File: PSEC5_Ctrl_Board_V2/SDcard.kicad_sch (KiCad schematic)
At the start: 27 parts, among them J3 1040310811, J6 1040310811, Q1 NMOS, Q4 NMOS, U14 SIA427ADJ-T1-GE3, U17 TXS02612RTWR, U6 SIA427ADJ-T1-GE3

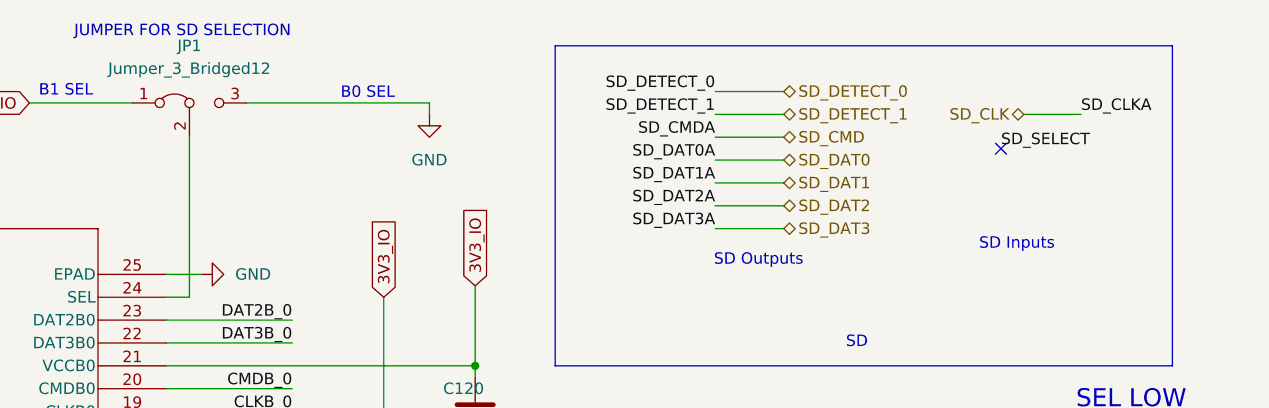
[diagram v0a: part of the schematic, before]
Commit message: Updated V2
New Power Planes, roruing of bottom samtec and kria positions
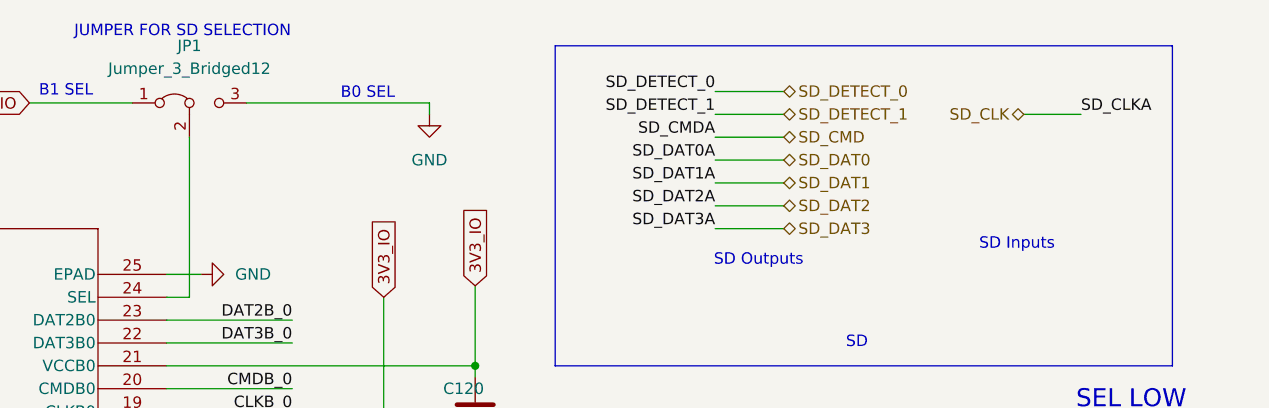
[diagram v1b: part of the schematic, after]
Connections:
- no-connect marks 1 -> 0

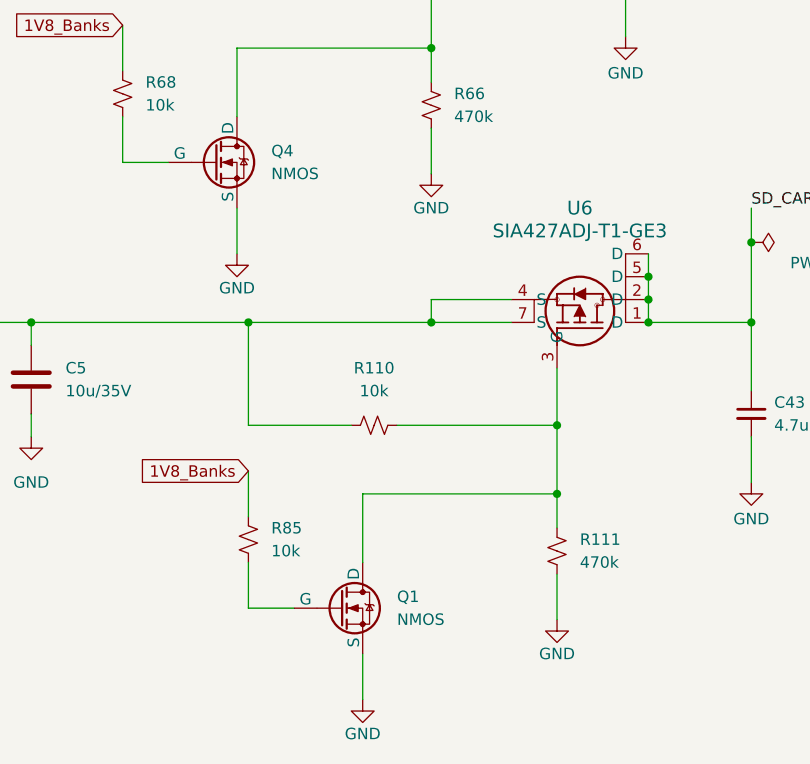
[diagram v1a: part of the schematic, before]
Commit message: Adjusted Footprints
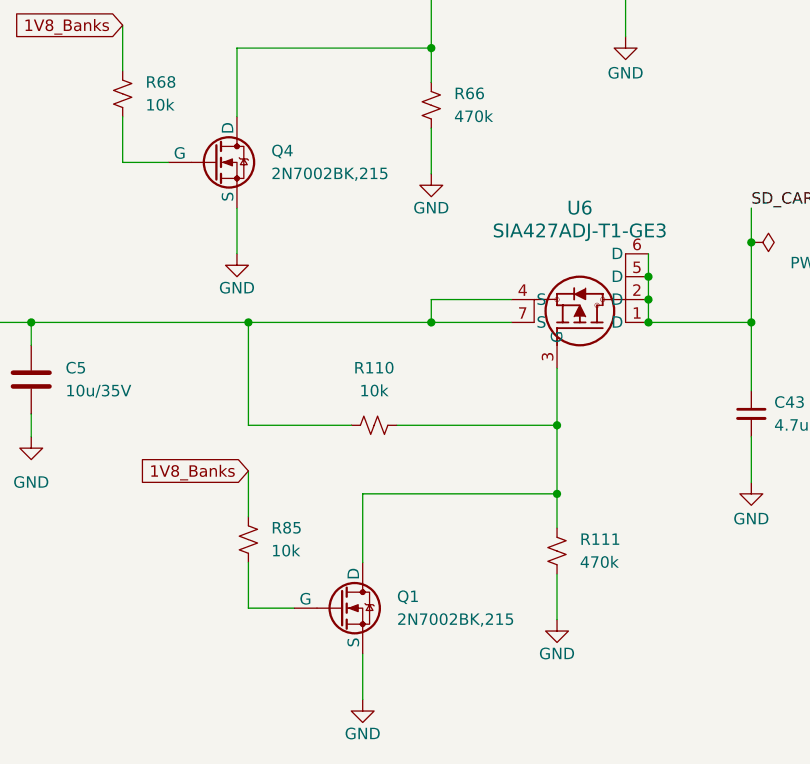
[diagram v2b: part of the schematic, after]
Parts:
- Q1, Q4: value NMOS -> 2N7002BK,215
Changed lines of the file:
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@@
 			)
 		)
-		(property "Value" "NMOS"
+		(property "Value" "2N7002BK,215"
 			(at 93.98 133.3499 0)
 			(effects
@@
 			)
 		)
-		(property "Datasheet" "https://ngspice.sourceforge.io/docs/ngspice-html-manual/manual.xhtml#cha_MOSFETs"
+		(property "Datasheet" "https://assets.nexperia.com/documents/data-sheet/2N7002BK.pdf"
 			(at 87.63 144.78 0)
 			(effects
@@
 			)
 		)
-		(property "Value" "NMOS"
+		(property "Value" "2N7002BK,215"
 			(at 107.95 182.8799 0)
 			(effects
